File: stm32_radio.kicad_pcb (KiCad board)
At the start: 2 copper layers, 88.9 x 82.5 mm, 62 parts, among them J1 Conn_01x03_Pin, J2 Conn_Coaxial_Small, J3 Conn_01x03_Pin, Q1 NDT3055L, Q2 FDN 306P, Q3 NMOS, Q4 NDT3055L, U1 STM32WL55CCU7, U2 AS179-92LF, U3 TPS2553DBVT-1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

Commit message: Almost ready for production
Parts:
- added D8: Green, LED_SMD:LED_0805_2012Metric, F.Cu at (154.5, 78.7)
- added R12: 100k, Resistor_SMD:R_0805_2012Metric, F.Cu at (176.8, 86.9)
- added R13: 470, Resistor_SMD:R_0805_2012Metric, F.Cu at (154.4, 80.8)
- D2: footprint Diode_SMD:D_2114_3652Metric -> Diode_SMD:D_SOD-323
- Q1: value NDT3055L -> ???; footprint Package_TO_SOT_SMD:SOT-223-3_TabPin2 -> Package_TO_SOT_SMD:SOT-23
- Q3: footprint Package_TO_SOT_SMD:SOT-23-3 -> Package_TO_SOT_SMD:SOT-23
- Q4: value NDT3055L -> Q_NPN; footprint Package_TO_SOT_SMD:SOT-223-3_TabPin2 -> Package_TO_SOT_SMD:SOT-23
- R10: value R -> 10k
- R11: value R -> 20k
- moved C23 17.6 mm to (128.5, 61.0)
- moved L5 17.6 mm to (130.3, 62.5)
- moved C22 17.6 mm to (128.6, 64.5)
- moved C14 16.9 mm to (131.1, 65.8)
- moved C17 16.9 mm to (133.1, 65.8)
- moved L2 16.9 mm to (132.1, 68.3)
- moved C19 15.1 mm to (152.7, 65.3)
- moved L6 15.1 mm to (156.7, 62.9)
- moved C13 15.1 mm to (160.0, 67.2)
- moved C18 15.1 mm to (154.7, 63.9)
- moved C21 15.1 mm to (157.5, 64.4)
- moved C24 15.1 mm to (158.8, 60.6)
- moved L3 15.1 mm to (155.4, 66.5)
- moved L4 15.1 mm to (158.8, 62.9)
- moved C16 15.1 mm to (158.1, 67.1)
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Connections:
- net /Radio MCU/LSW/nFault renamed /Radio MCU/LSW/nFAULT
- Q4 pad 1: Net-(Q4-G) -> Net-(Q4-B)
- Q4 pad 2: /Radio MCU/VBAT -> Net-(Q4-E)
- Q4 pad 3: Net-(Q4-S) -> /Radio MCU/VBAT
- R11 pad 1: Net-(Q4-S) -> Net-(U1-PB3)
- R11 pad 2: Net-(U1-PB3) -> Net-(Q4-E)
- U1 pad 13: Net-(Q4-G) -> Net-(U1-PA5)
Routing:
- net Net-(U1-PA5): track 0.00 -> 35.0 mm, vias 0 -> 2
- net Net-(Q4-G): track 34.1 -> 0.00 mm, vias 2 -> 0
- net /Radio MCU/RF out/TX_EN: track 23.0 -> 49.4 mm
- net /Radio MCU/RF out/RX_EN: track 23.2 -> 48.3 mm, vias 2 -> 0
- net Net-(U1-OSC_IN): track 2.85 -> 18.6 mm, vias 0 -> 2
- net GND: track 43.4 -> 29.0 mm, vias 20 -> 24
- net /Radio MCU/3V3: track 153.4 -> 167.2 mm, vias 9 -> 10
- net /Radio MCU/VBAT: track 32.8 -> 20.5 mm
- net /Radio MCU/UART2_RX: track 33.1 -> 21.3 mm
- net /Radio MCU/RF out/RF_RX: track 6.00 -> 16.4 mm
- net /Radio MCU/RF out/RFO_HP: track 17.6 -> 27.8 mm, vias 0 -> 2
- net /Radio MCU/RF out/VR_PA: track 15.6 -> 24.2 mm, vias 0 -> 2
- net /Radio MCU/RF out/RFI_P: track 15.5 -> 23.3 mm
- net /Radio MCU/RF out/RFI_N: track 15.9 -> 23.0 mm
- net /Radio MCU/UART2_TX: track 19.4 -> 26.0 mm
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
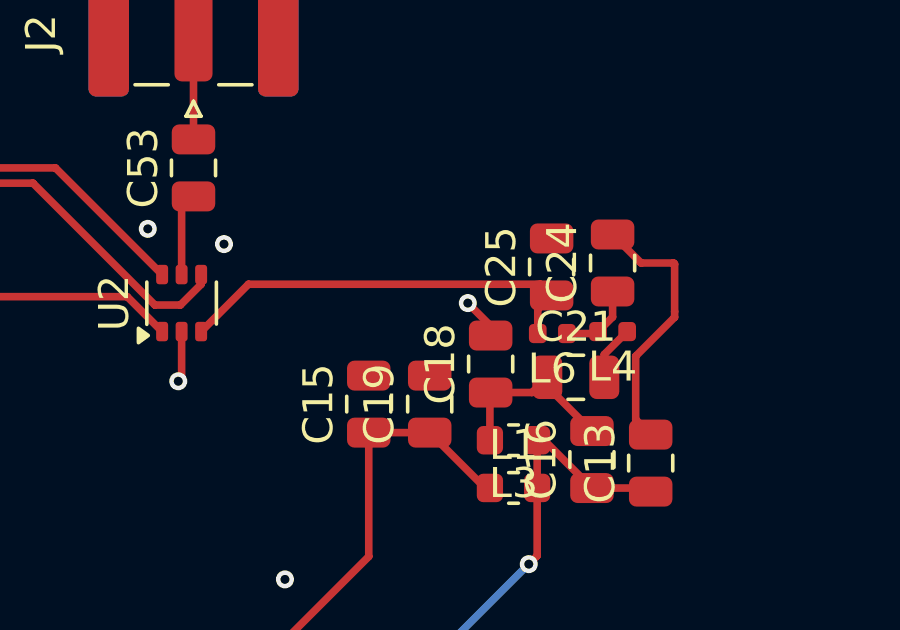
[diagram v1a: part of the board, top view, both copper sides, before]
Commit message: Fix footprints
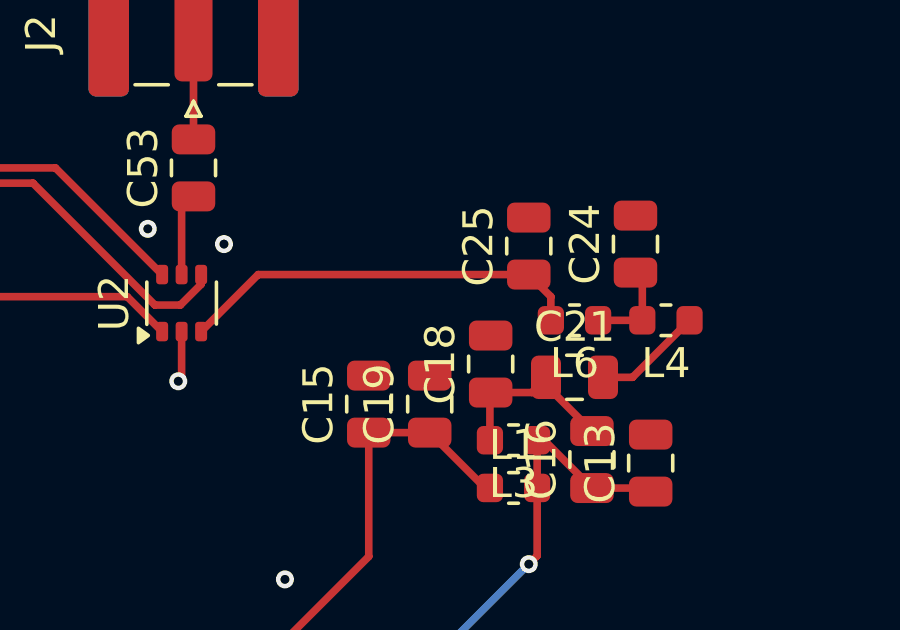
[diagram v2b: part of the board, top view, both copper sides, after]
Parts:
- L4, L6: footprint Inductor_SMD:L_0402_1005Metric -> Inductor_SMD:L_0603_1608Metric
- moved L4 1.82 mm to (160.5, 62.5)
- moved C25 1.03 mm to (156.0, 60.0)
- moved C24 0.99 mm to (159.5, 59.9)
- moved L6 0.86 mm to (157.5, 62.5)
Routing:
- net GND: track 29.0 -> 18.7 mm, vias 24 -> 23
- net /Radio MCU/RF out/50ohm_2: track 1.84 -> 3.67 mm
- net /Radio MCU/RF out/50ohm_3: track 2.60 -> 3.16 mm

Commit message: Finalize design
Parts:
- removed C26: 100n, Capacitor_SMD:C_0805_2012Metric
- removed D7: Green, LED_SMD:LED_1206_3216Metric
- removed D8: Green, LED_SMD:LED_0805_2012Metric
- removed J1: Conn_01x03_Pin, Connector_PinHeader_2.54mm:PinHeader_1x03_P2.54mm_Vertical
- removed Q1: ???, Package_TO_SOT_SMD:SOT-23
- removed Q3: NMOS, Package_TO_SOT_SMD:SOT-23
- removed R13: 470, Resistor_SMD:R_0805_2012Metric
- removed R7: 180k, Resistor_SMD:R_1206_3216Metric
- removed R8: 13k, Resistor_SMD:R_0603_1608Metric
- removed R9: 150, Resistor_SMD:R_0805_2012Metric
- removed U3: TPS2553DBVT-1, Package_TO_SOT_SMD:SOT-23-6
- D5, D6: value BAT54W-HG3-08 -> Green; footprint Diode_SMD:D_SOD-123 -> LED_SMD:LED_0805_2012Metric
- L4: value 21n -> 22n
- Q2: value FDN 306P -> DMN1019USN-7
- R5: value 180k -> 470; footprint Resistor_SMD:R_1206_3216Metric -> Resistor_SMD:R_0805_2012Metric
- R6: value 1k -> 470
- moved R6 64.6 mm to (118.8, 69.8), turned to 180 degrees
- moved R5 59.6 mm to (118.8, 72.8), turned to 180 degrees
- moved D5 49.5 mm to (123.2, 72.8)
- moved D6 48.8 mm to (123.2, 69.7), turned to 0 degrees
- moved Q2 30.4 mm to (154.2, 84.1)
- moved C14 23.4 mm to (154.4, 67.3)
- moved C17 23.4 mm to (156.5, 67.3)
- moved C22 23.4 mm to (151.9, 66.0)
- moved C23 23.4 mm to (151.9, 62.5)
- moved L2 23.4 mm to (155.4, 69.8)
- moved L5 23.4 mm to (153.7, 64.0)
- moved L4 22.5 mm to (138.2, 64.8), turned to 90 degrees
- moved L1 22.0 mm to (133.5, 68.9)
- moved L3 22.0 mm to (133.5, 67.3)
- moved C16 21.9 mm to (136.1, 68.1)
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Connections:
- B1 pad 25: /Radio MCU/Power EN -> /Power EN
- B1 pad 27: /Radio MCU/LSW/nFAULT -> /nFAULT
- B1 pad 5: INPUT +3.3V -> /Radio MCU/3V3
- B1 pad 6: INPUT +3.3V -> /Radio MCU/3V3
- D5 pad 2: Net-(D5-A) -> /Radio MCU/RF out/RX_EN
- D6 pad 2: /Radio MCU/LSW/nFAULT -> /Radio MCU/RF out/TX_EN
- Q2 pad 1: Net-(D5-K) -> /Radio MCU/UART2_TX
- Q2 pad 2: INPUT +3.3V -> GND
- Q2 pad 3: Net-(Q2-D) -> /Radio MCU/UART
- Q4 pad 3: /Radio MCU/VBAT -> Net-(Q4-C)
- R10 pad 1: Net-(U1-PB3) -> Net-(Q4-E)
- R11 pad 1: Net-(U1-PB3) -> Net-(Q4-C)
- R11 pad 2: Net-(Q4-E) -> /Radio MCU/VBAT
- R5 pad 2: INPUT +3.3V -> GND
- R6 pad 1: /Radio MCU/Power EN -> Net-(D6-K)
- R6 pad 2: Net-(D5-K) -> GND
- U1 pad 1: Net-(U1-PB3) -> Net-(Q4-E)
- U2 pad 1: /Radio MCU/RF out/RF_RX -> /Radio MCU/RF out/RF_TX
- U2 pad 3: /Radio MCU/RF out/RF_TX -> /Radio MCU/RF out/RF_RX
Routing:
- net /Radio MCU/LSW/nFAULT: track 74.0 -> 0.00 mm, vias 2 -> 0
- net /Radio MCU/Power EN: track 68.7 -> 0.00 mm, vias 1 -> 0
- net INPUT +3.3V: track 54.1 -> 0.00 mm, vias 2 -> 0
- net Net-(U1-PB3): track 47.0 -> 0.00 mm, vias 2 -> 0
- net Net-(Q4-E): track 1.92 -> 48.2 mm, vias 0 -> 2
- net Net-(D5-K): track 37.9 -> 2.58 mm, vias 2 -> 0
- net Net-(Q2-D): track 28.4 -> 0.00 mm, vias 3 -> 0
- net Net-(D5-A): track 16.0 -> 0.00 mm
- net /Radio MCU/3V3: track 167.2 -> 153.7 mm, vias 10 -> 9
- net Net-(D6-K): track 15.8 -> 2.62 mm, vias 2 -> 0
- net GND: track 18.7 -> 31.0 mm, vias 23 -> 34
- net /Radio MCU/UART: track 68.5 -> 59.6 mm
- net Net-(D4-A): track 11.7 -> 4.49 mm
- net /Radio MCU/RF out/TX_EN: track 49.4 -> 56.3 mm, vias 0 -> 2
- net /Radio MCU/RF out/RF_RX: track 16.4 -> 9.88 mm
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
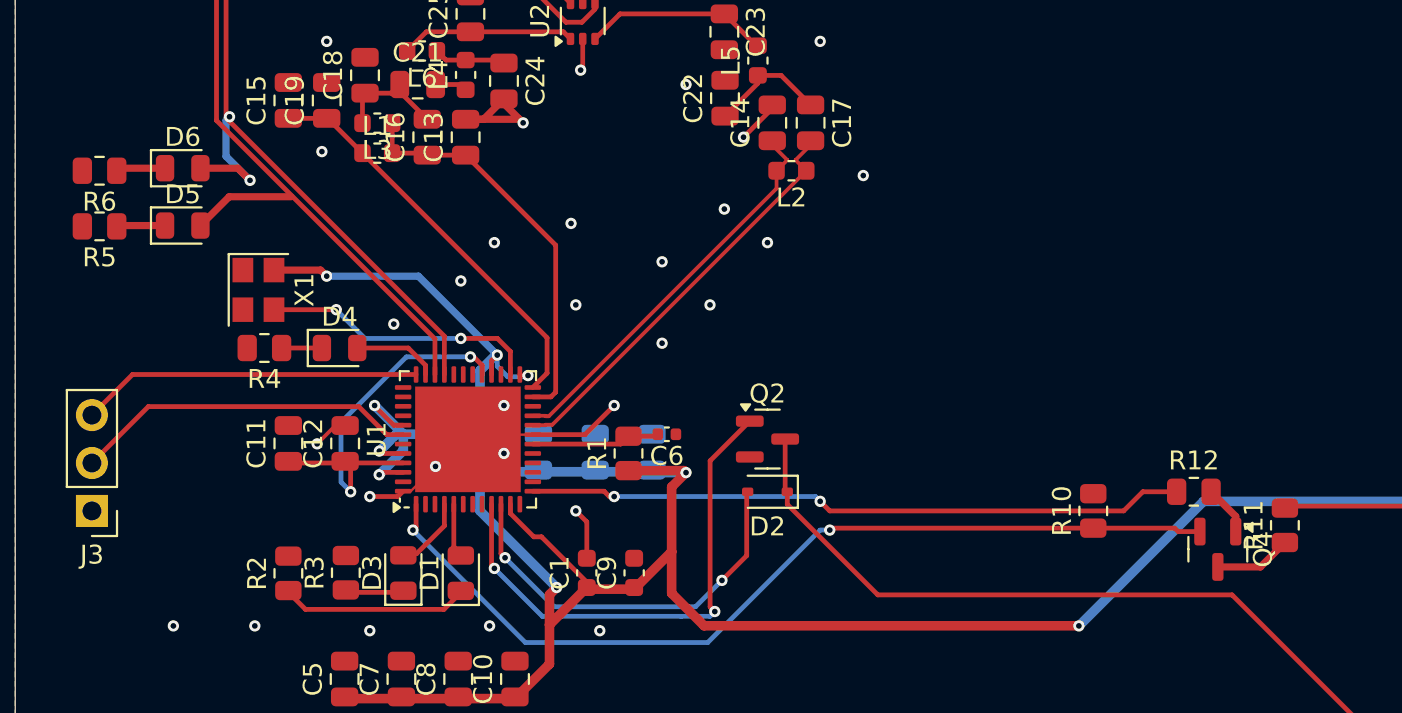
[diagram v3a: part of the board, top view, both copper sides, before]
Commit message: Altered LCSC part numbers according to current stock
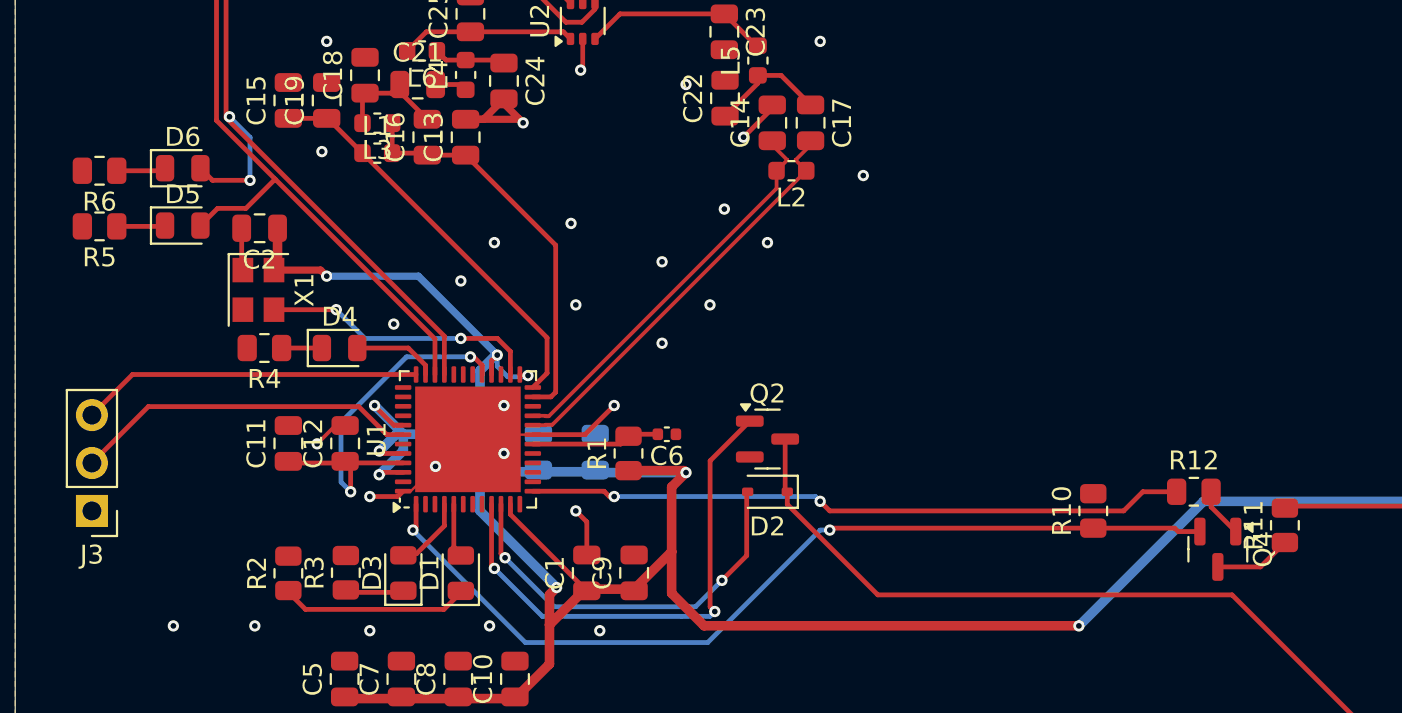
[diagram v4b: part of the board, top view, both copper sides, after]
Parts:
- C1, C9: footprint Capacitor_SMD:C_0603_1608Metric -> Capacitor_SMD:C_0805_2012Metric
- C2: value 1n -> 12p; moved to F.Cu
- moved C2 24.0 mm to (127.3, 72.9), turned to 180 degrees
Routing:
- net GND: track 31.0 -> 33.2 mm
- net /Radio MCU/3V3: track 153.7 -> 155.9 mm

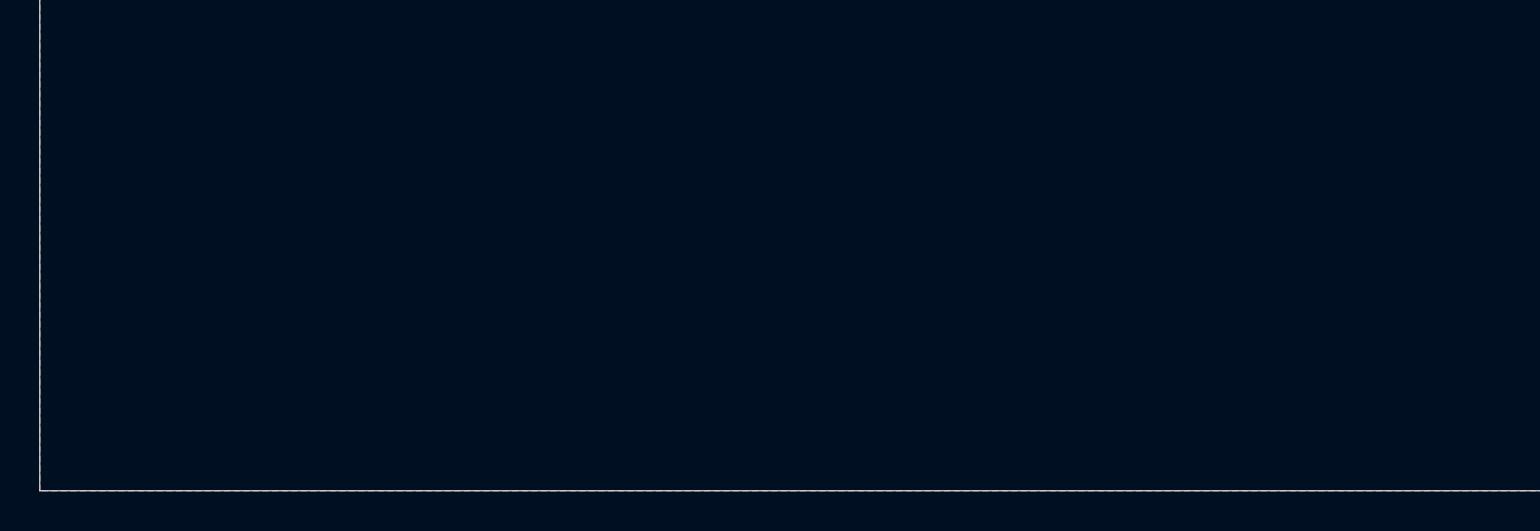
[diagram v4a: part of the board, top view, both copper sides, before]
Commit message: Added a pair of SMA connectors for measurement
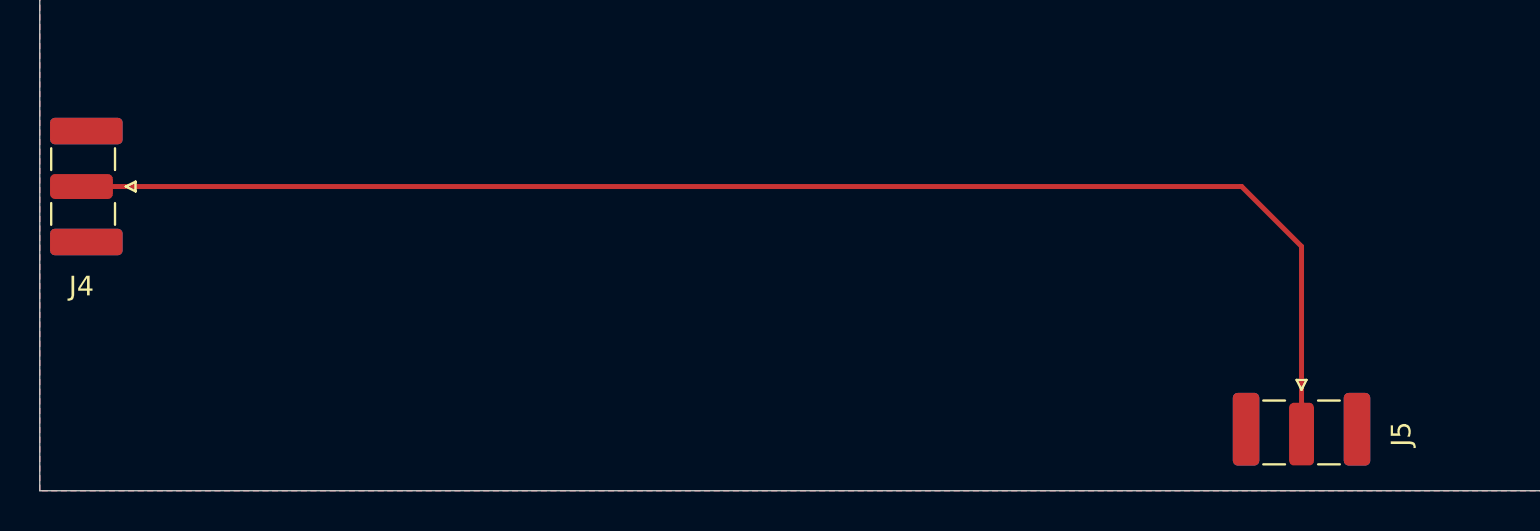
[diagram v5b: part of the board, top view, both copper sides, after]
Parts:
- added J4: Conn_Coaxial_Small, Connector_Coaxial:SMA_Samtec_SMA-J-P-H-ST-EM1_EdgeMount, F.Cu at (116.4, 117.9)
- added J5: Conn_Coaxial_Small, Connector_Coaxial:SMA_Samtec_SMA-J-P-H-ST-EM1_EdgeMount, F.Cu at (178.6, 130.5)
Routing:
- net /50_ohm_test: track 0.00 -> 73.0 mm
